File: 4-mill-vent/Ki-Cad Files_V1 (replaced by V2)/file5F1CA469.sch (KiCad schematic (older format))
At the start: 15 parts, among them J6 Charger_Port, J8 Board_Power

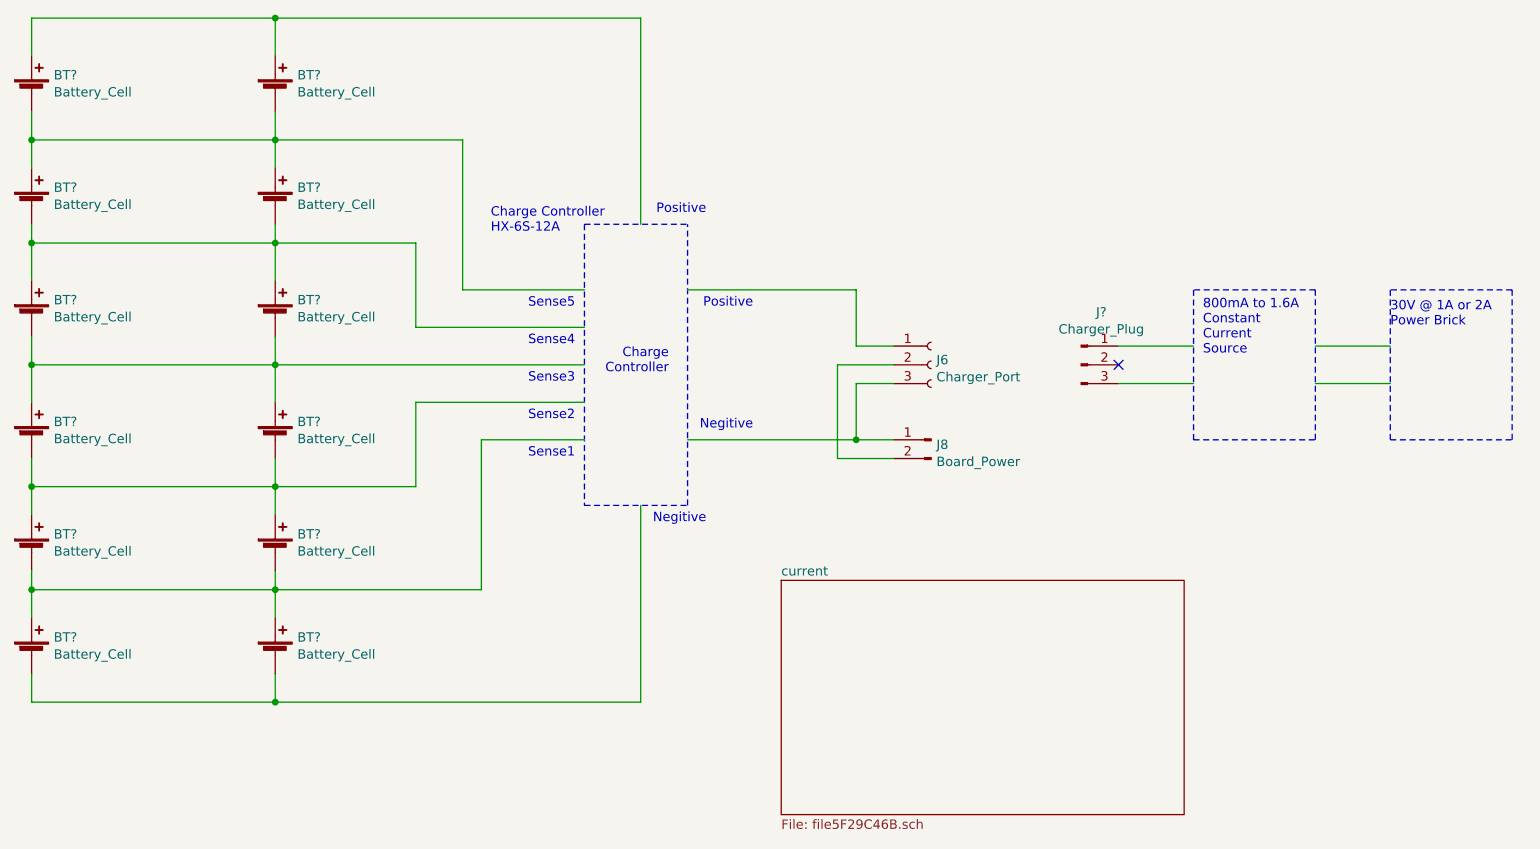
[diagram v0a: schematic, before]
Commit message: Last Update USE V2
Board test complete, all slikscreen error are fixed in v2, Full use of opamp for battery monitoring.
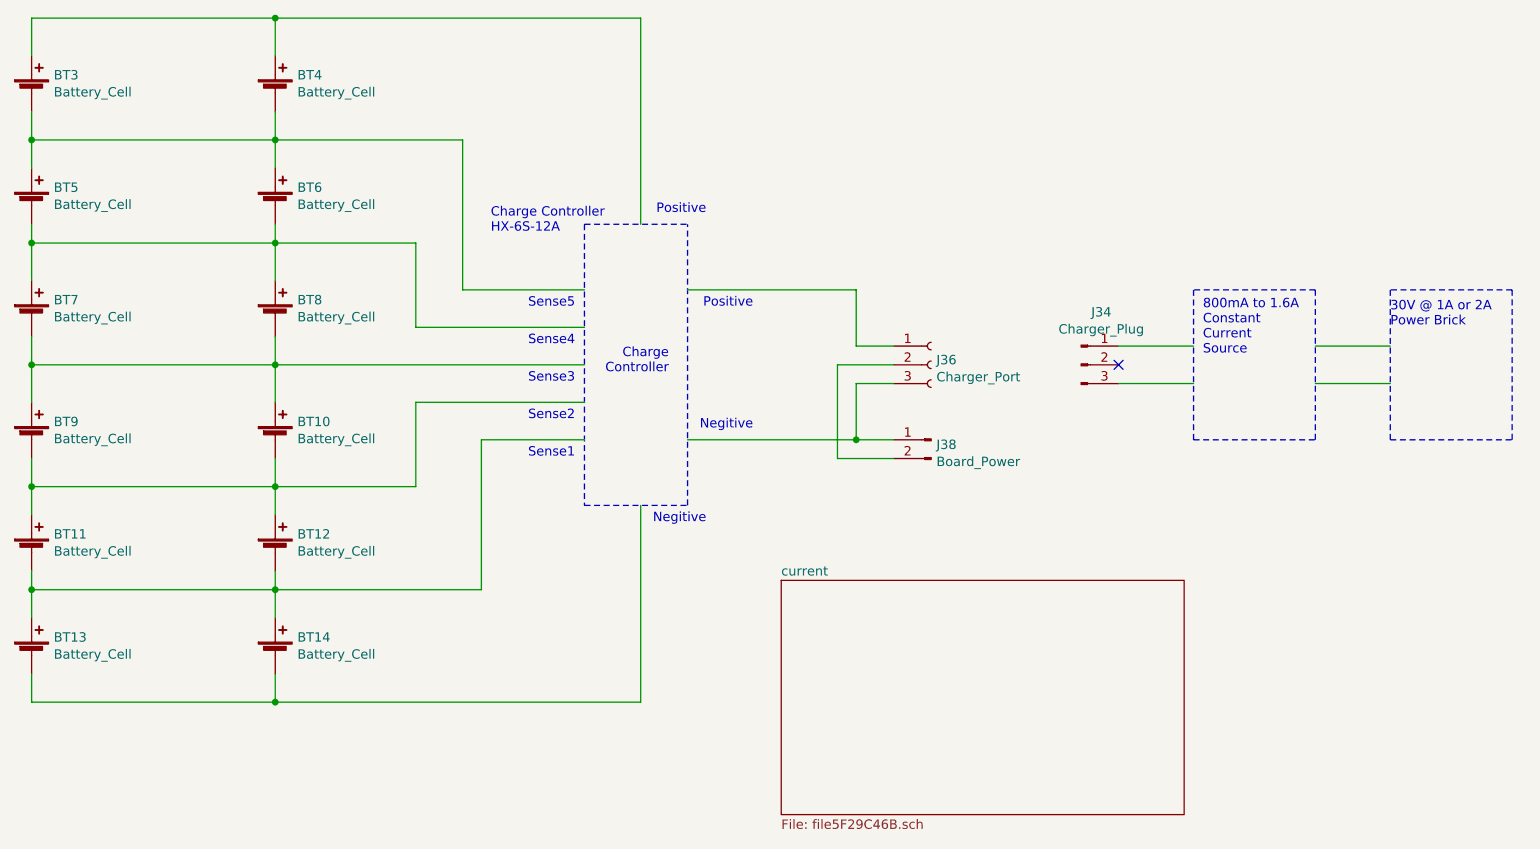
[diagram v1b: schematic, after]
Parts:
- gave numbers to parts that had none: 13
- renumbered J6 to J36, J8 to J38
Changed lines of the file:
@@
 $EndDescr
 $Comp
-L Device:Battery_Cell BT?
+L Device:Battery_Cell BT3
 U 1 1 5F1CA824
 P 1050 2200
-F 0 "BT?" H 1168 2296 50  0000 L CNN
+F 0 "BT3" H 1168 2296 50  0000 L CNN
 F 1 "Battery_Cell" H 1168 2205 50  0000 L CNN
 F 2 "" V 1050 2260 50  0001 C CNN
@@
 $EndComp
 $Comp
-L Device:Battery_Cell BT?
+L Device:Battery_Cell BT5
 U 1 1 5F1CB129
 P 1050 2800
-F 0 "BT?" H 1168 2896 50  0000 L CNN
+F 0 "BT5" H 1168 2896 50  0000 L CNN
 F 1 "Battery_Cell" H 1168 2805 50  0000 L CNN
 F 2 "" V 1050 2860 50  0001 C CNN
@@
 $EndComp
 $Comp
-L Device:Battery_Cell BT?
+L Device:Battery_Cell BT7
 U 1 1 5F1CBE25
 P 1050 3400
-F 0 "BT?" H 1168 3496 50  0000 L CNN
+F 0 "BT7" H 1168 3496 50  0000 L CNN
 F 1 "Battery_Cell" H 1168 3405 50  0000 L CNN
 F 2 "" V 1050 3460 50  0001 C CNN
@@
 $EndComp
 $Comp
-L Device:Battery_Cell BT?
+L Device:Battery_Cell BT9
 U 1 1 5F1CEC7A
 P 1050 4050
-F 0 "BT?" H 1168 4146 50  0000 L CNN
+F 0 "BT9" H 1168 4146 50  0000 L CNN
 F 1 "Battery_Cell" H 1168 4055 50  0000 L CNN
 F 2 "" V 1050 4110 50  0001 C CNN
@@
 $EndComp
 $Comp
-L Device:Battery_Cell BT?
+L Device:Battery_Cell BT11
 U 1 1 5F1CEC80
 P 1050 4650
-F 0 "BT?" H 1168 4746 50  0000 L CNN
+F 0 "BT11" H 1168 4746 50  0000 L CNN
 F 1 "Battery_Cell" H 1168 4655 50  0000 L CNN
 F 2 "" V 1050 4710 50  0001 C CNN
@@
 $EndComp
 $Comp
-L Device:Battery_Cell BT?
+L Device:Battery_Cell BT13
 U 1 1 5F1CEC86
 P 1050 5200
-F 0 "BT?" H 1168 5296 50  0000 L CNN
+F 0 "BT13" H 1168 5296 50  0000 L CNN
 F 1 "Battery_Cell" H 1168 5205 50  0000 L CNN
 F 2 "" V 1050 5260 50  0001 C CNN
@@
 $EndComp
 $Comp
-L Device:Battery_Cell BT?
+L Device:Battery_Cell BT4
 U 1 1 5F1D904E
 P 2350 2200
-F 0 "BT?" H 2468 2296 50  0000 L CNN
+F 0 "BT4" H 2468 2296 50  0000 L CNN
 F 1 "Battery_Cell" H 2468 2205 50  0000 L CNN
 F 2 "" V 2350 2260 50  0001 C CNN
@@
 $EndComp
 $Comp
-L Device:Battery_Cell BT?
+L Device:Battery_Cell BT6
 U 1 1 5F1D9054
 P 2350 2800
-F 0 "BT?" H 2468 2896 50  0000 L CNN
+F 0 "BT6" H 2468 2896 50  0000 L CNN
 F 1 "Battery_Cell" H 2468 2805 50  0000 L CNN
 F 2 "" V 2350 2860 50  0001 C CNN
@@
 $EndComp
 $Comp
-L Device:Battery_Cell BT?
+L Device:Battery_Cell BT8
 U 1 1 5F1D905A
 P 2350 3400
-F 0 "BT?" H 2468 3496 50  0000 L CNN
+F 0 "BT8" H 2468 3496 50  0000 L CNN
 F 1 "Battery_Cell" H 2468 3405 50  0000 L CNN
 F 2 "" V 2350 3460 50  0001 C CNN
@@
 $EndComp
 $Comp
-L Device:Battery_Cell BT?
+L Device:Battery_Cell BT10
 U 1 1 5F1D9060
 P 2350 4050
-F 0 "BT?" H 2468 4146 50  0000 L CNN
+F 0 "BT10" H 2468 4146 50  0000 L CNN
 F 1 "Battery_Cell" H 2468 4055 50  0000 L CNN
 F 2 "" V 2350 4110 50  0001 C CNN
@@
 $EndComp
 $Comp
-L Device:Battery_Cell BT?
+L Device:Battery_Cell BT12
 U 1 1 5F1D9066
 P 2350 4650
-F 0 "BT?" H 2468 4746 50  0000 L CNN
+F 0 "BT12" H 2468 4746 50  0000 L CNN
 F 1 "Battery_Cell" H 2468 4655 50  0000 L CNN
 F 2 "" V 2350 4710 50  0001 C CNN
@@
 $EndComp
 $Comp
-L Device:Battery_Cell BT?
+L Device:Battery_Cell BT14
 U 1 1 5F1D906C
 P 2350 5200
-F 0 "BT?" H 2468 5296 50  0000 L CNN
+F 0 "BT14" H 2468 5296 50  0000 L CNN
 F 1 "Battery_Cell" H 2468 5205 50  0000 L CNN
 F 2 "" V 2350 5260 50  0001 C CNN
@@
 	4000 2900 4550 2900
 $Comp
-L Connector:Conn_01x03_Female J6
+L Connector:Conn_01x03_Female J36
 U 1 1 5F1EDD5E
 P 5850 3650
-F 0 "J6" H 5878 3676 50  0000 L CNN
+F 0 "J36" H 5878 3676 50  0000 L CNN
 F 1 "Charger_Port" H 5878 3585 50  0000 L CNN
 F 2 "" H 5850 3650 50  0001 C CNN
@@
 	5350 4150 5650 4150
 $Comp
-L Connector:Conn_01x02_Male J8
+L Connector:Conn_01x02_Male J38
 U 1 1 5F1F487A
 P 5850 4050
-F 0 "J8" H 5822 4024 50  0000 R CNN
+F 0 "J38" H 5822 4024 50  0000 R CNN
 F 1 "Board_Power" H 5822 3933 50  0000 R CNN
 F 2 "" H 5850 4050 50  0001 C CNN
@@
 Charge\nController
 $Comp
-L Connector:Conn_01x03_Male J?
+L Connector:Conn_01x03_Male J34
 U 1 1 5F290A6E
 P 6650 3650
-F 0 "J?" H 6758 3931 50  0000 C CNN
+F 0 "J34" H 6758 3931 50  0000 C CNN
 F 1 "Charger_Plug" H 6758 3840 50  0000 C CNN
 F 2 "" H 6650 3650 50  0001 C CNN
